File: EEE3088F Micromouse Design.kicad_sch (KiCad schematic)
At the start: 65 parts, among them J1 Conn_02x16_Odd_Even, J2 Conn_01x02, J3 TYPE-C-31-M-12, Q2 AO3400A, SW1 SW_SPDT, U1 INA219AxD, U11 DRV8833PW, U12 DRV8833PW, U13 AP22966DC8-7, U15 TP4056-42-ESOP8, U6 TPS5430DDA, U7 TPS61088RHLR, U9 CH224K

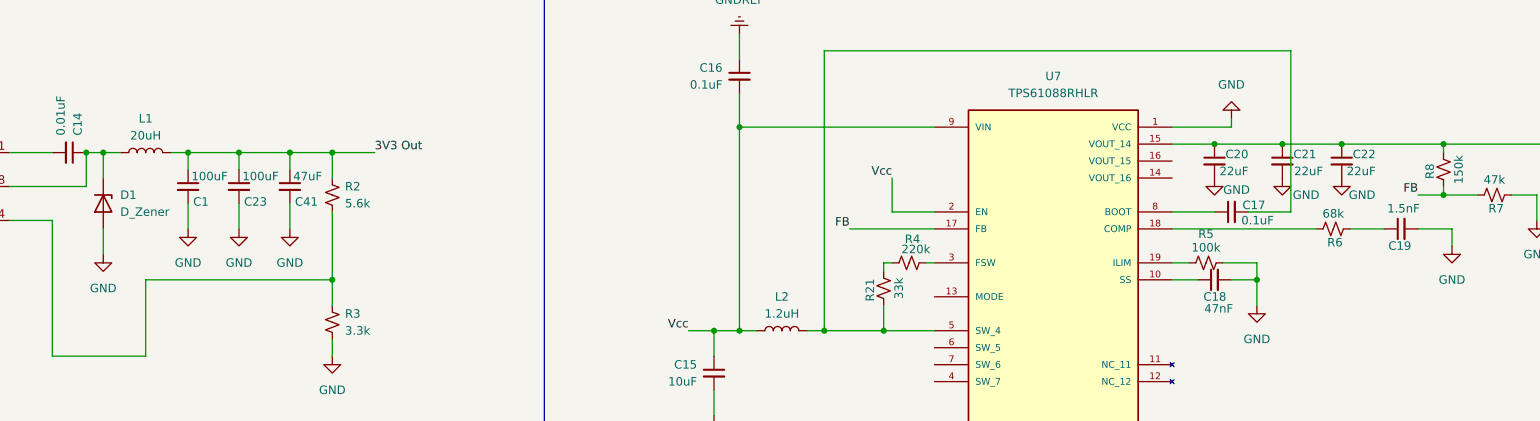
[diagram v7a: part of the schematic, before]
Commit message: Added footprints to 2 of 3 subcircuits
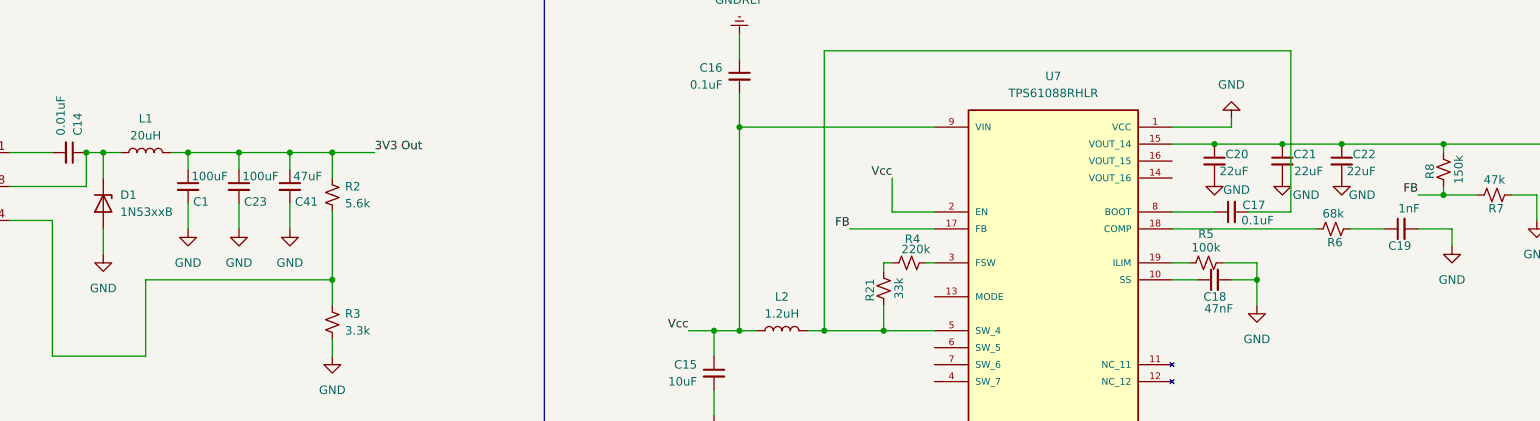
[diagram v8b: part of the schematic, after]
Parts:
- removed D1: D_Zener, symbol Device:D_Zener
- added D1: 1N53xxB, Inductor_1.2uH:L_custom_SMD, symbol Diode:1N53xxB
- C1, C23: footprint (none) -> Capacitor_SMD:C_1206_3216Metric_Pad1.33x1.80mm_HandSolder
- C14: footprint Capacitor_SMD:C_0402_1005Metric_Pad0.74x0.62mm_HandSolder -> Capacitor_SMD:C_0805_2012Metric_Pad1.18x1.45mm_HandSolder
- C15, C20: footprint Capacitor_SMD:C_0402_1005Metric_Pad0.74x0.62mm_HandSolder -> Capacitor_SMD:C_1206_3216Metric
- C18: footprint Capacitor_SMD:C_0402_1005Metric_Pad0.74x0.62mm_HandSolder -> Capacitor_SMD:C_0603_1608Metric_Pad1.08x0.95mm_HandSolder
- C19: value 1.5nF -> 1nF; footprint Capacitor_SMD:C_0402_1005Metric_Pad0.74x0.62mm_HandSolder -> Capacitor_SMD:C_0805_2012Metric_Pad1.18x1.45mm_HandSolder
- C21, C22: footprint Capacitor_SMD:C_0402_1005Metric_Pad0.74x0.62mm_HandSolder -> Capacitor_SMD:C_1206_3216Metric_Pad1.33x1.80mm_HandSolder
- C41: footprint (none) -> Capacitor_SMD:C_0805_2012Metric_Pad1.18x1.45mm_HandSolder
- L1: footprint (none) -> Inductor_THT:L_Axial_L11.0mm_D4.5mm_P5.08mm_Vertical_Fastron_MECC
- L2: footprint (none) -> Inductor_SMD:L_Changjiang_FXL0420
- R1: footprint Resistor_SMD:R_1206_3216Metric_Pad1.30x1.75mm_HandSolder -> Resistor_SMD:R_2512_6332Metric
- R16: footprint Resistor_SMD:R_1206_3216Metric_Pad1.30x1.75mm_HandSolder -> Resistor_SMD:R_2512_6332Metric_Pad1.40x3.35mm_HandSolder
- R2, R3, R4, R7, R8: footprint Resistor_SMD:R_1206_3216Metric_Pad1.30x1.75mm_HandSolder -> Resistor_SMD:R_0805_2012Metric_Pad1.20x1.40mm_HandSolder
- R6: footprint Resistor_SMD:R_1206_3216Metric_Pad1.30x1.75mm_HandSolder -> Resistor_SMD:R_0805_2012Metric
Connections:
- net GND: now also D1.2 (A)
- net at C14.1, L1.1, U6.8 (PH): now also D1.1 (K)
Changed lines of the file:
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@@
 			)
 		)
-		(property "Footprint" ""
+		(property "Footprint" "Inductor_THT:L_Axial_L11.0mm_D4.5mm_P5.08mm_Vertical_Fastron_MECC"
 			(at 269.24 52.07 0)
 			(effects
@@
 			)
 		)
-		(property "Footprint" "Resistor_SMD:R_1206_3216Metric_Pad1.30x1.75mm_HandSolder"
+		(property "Footprint" "Resistor_SMD:R_0805_2012Metric_Pad1.20x1.40mm_HandSolder"
 			(at 383.54 68.58 0)
 			(effects
@@
 			)
 		)
-		(property "Footprint" "Capacitor_SMD:C_0402_1005Metric_Pad0.74x0.62mm_HandSolder"
+		(property "Footprint" "Capacitor_SMD:C_1206_3216Metric"
 			(at 429.26 53.34 0)
 			(effects
@@
 			)
 		)
-		(property "Footprint" "Capacitor_SMD:C_0402_1005Metric_Pad0.74x0.62mm_HandSolder"
+		(property "Footprint" "Capacitor_SMD:C_1206_3216Metric_Pad1.33x1.80mm_HandSolder"
 			(at 448.31 53.34 0)
 			(effects
@@
 			)
 		)
-		(property "Footprint" "Resistor_SMD:R_1206_3216Metric_Pad1.30x1.75mm_HandSolder"
+		(property "Footprint" "Resistor_SMD:R_0805_2012Metric_Pad1.20x1.40mm_HandSolder"
 			(at 471.17 58.42 0)
 			(effects
@@
 			)
 		)
-		(property "Footprint" "Resistor_SMD:R_1206_3216Metric_Pad1.30x1.75mm_HandSolder"
+		(property "Footprint" "Resistor_SMD:R_0805_2012Metric_Pad1.20x1.40mm_HandSolder"
 			(at 297.18 77.47 0)
 			(effects
@@
 			)
 		)
-		(property "Footprint" "Resistor_SMD:R_1206_3216Metric_Pad1.30x1.75mm_HandSolder"
+		(property "Footprint" "Resistor_SMD:R_0805_2012Metric_Pad1.20x1.40mm_HandSolder"
 			(at 463.55 54.61 0)
 			(effects
@@
 			)
 		)
-		(property "Footprint" "Capacitor_SMD:C_0402_1005Metric_Pad0.74x0.62mm_HandSolder"
+		(property "Footprint" "Capacitor_SMD:C_1206_3216Metric"
 			(at 354.33 85.09 0)
 			(effects
@@
 			)
 		)
-		(property "Footprint" ""
+		(property "Footprint" "Capacitor_SMD:C_1206_3216Metric_Pad1.33x1.80mm_HandSolder"
 			(at 275.59 57.15 0)
 			(effects
@@
 			)
 		)
-		(property "Footprint" "Capacitor_SMD:C_0402_1005Metric_Pad0.74x0.62mm_HandSolder"
+		(property "Footprint" "Capacitor_SMD:C_0603_1608Metric_Pad1.08x0.95mm_HandSolder"
 			(at 429.26 71.12 0)
 			(effects
@@
 			)
 		)
-		(property "Footprint" "Resistor_SMD:R_1206_3216Metric_Pad1.30x1.75mm_HandSolder"
+		(property "Footprint" "Resistor_SMD:R_0805_2012Metric_Pad1.20x1.40mm_HandSolder"
 			(at 297.18 58.42 0)
 			(effects
@@
 			)
 		)
-		(property "Footprint" "Resistor_SMD:R_1206_3216Metric_Pad1.30x1.75mm_HandSolder"
+		(property "Footprint" "Resistor_SMD:R_2512_6332Metric"
 			(at 130.81 62.23 0)
 			(effects
@@
 	)
 	(symbol
+		(lib_id "Diode:1N53xxB")
+		(at 262.89 59.69 270)
+		(unit 1)
+		(exclude_from_sim no)
+		(in_bom yes)
+		(on_board yes)
+		(dnp no)
+		(fields_autoplaced yes)
+		(property "Reference" "D1"
+			(at 265.43 58.4199 90)
+			(effects
+				(font
+					(size 1.27 1.27)
+				)
+				(justify left)
+			)
+		)
+		(property "Value" "1N53xxB"
+			(at 265.43 60.9599 90)
+			(effects
+				(font
+					(size 1.27 1.27)
+				)
+				(justify left)
+			)
+		)
+		(property "Footprint" "Inductor_1.2uH:L_custom_SMD"
+			(at 258.445 59.69 0)
+			(effects
+				(font
+					(size 1.27 1.27)
+				)
+				(hide yes)
+			)
+		)
+		(property "Datasheet" "https://diotec.com/tl_files/diotec/files/pdf/datasheets/1n5345b.pdf"
+			(at 262.89 59.69 0)
+			(effects
+				(font
+					(size 1.27 1.27)
+				)
+				(hide yes)
+			)
+		)
+		(property "Description" "5000mW Zener Diode, DO-201"
+			(at 262.89 59.69 0)
+			(effects
+				(font
+					(size 1.27 1.27)
+				)
+				(hide yes)
+			)
+		)
+		(pin "1"
+		)
+		(pin "2"
+		)
+		(instances
+			(project ""
+				(path "/9da86a77-c081-4eef-8f80-aa4f3cdcfcf8"
+					(reference "D1")
+					(unit 1)
+				)
+			)
+		)
+	)
+	(symbol
 		(lib_id "Device:C_Small")
 		(at 439.42 53.34 0)
@@
 			)
 		)
-		(property "Footprint" "Capacitor_SMD:C_0402_1005Metric_Pad0.74x0.62mm_HandSolder"
+		(property "Footprint" "Capacitor_SMD:C_1206_3216Metric_Pad1.33x1.80mm_HandSolder"
 			(at 439.42 53.34 0)
 			(effects
@@
 			)
 		)
-		(property "Footprint" ""
+		(property "Footprint" "Capacitor_SMD:C_1206_3216Metric_Pad1.33x1.80mm_HandSolder"
 			(at 283.21 57.15 0)
 			(effects
@@
 	)
 	(symbol
-		(lib_id "Device:D_Zener")
-		(at 262.89 59.69 270)
-		(unit 1)
-		(exclude_from_sim no)
-		(in_bom yes)
-		(on_board yes)
-		(dnp no)
-		(fields_autoplaced yes)
-		(property "Reference" "D1"
-			(at 265.43 58.4199 90)
-			(effects
-				(font
-					(size 1.27 1.27)
-				)
-				(justify left)
-			)
-		)
-		(property "Value" "D_Zener"
-			(at 265.43 60.9599 90)
-			(effects
-				(font
-					(size 1.27 1.27)
-				)
-				(justify left)
-			)
-		)
-		(property "Footprint" ""
-			(at 262.89 59.69 0)
-			(effects
-				(font
-					(size 1.27 1.27)
-				)
-				(hide yes)
-			)
-		)
-		(property "Datasheet" "~"
-			(at 262.89 59.69 0)
-			(effects
-				(font
-					(size 1.27 1.27)
-				)
-				(hide yes)
-			)
-		)
-		(property "Description" "Zener diode"
-			(at 262.89 59.69 0)
-			(effects
-				(font
-					(size 1.27 1.27)
-				)
-				(hide yes)
-			)
-		)
-		(pin "2"
-		)
-		(pin "1"
-		)
-		(instances
-			(project ""
-				(path "/9da86a77-c081-4eef-8f80-aa4f3cdcfcf8"
-					(reference "D1")
-					(unit 1)
-				)
-			)
-		)
-	)
-	(symbol
 		(lib_name "GND_12")
 		(lib_id "power:GND")
@@
 			)
 		)
-		(property "Footprint" ""
+		(property "Footprint" "Capacitor_SMD:C_0805_2012Metric_Pad1.18x1.45mm_HandSolder"
 			(at 290.83 57.15 0)
 			(effects
@@
 			)
 		)
-		(property "Footprint" "Resistor_SMD:R_1206_3216Metric_Pad1.30x1.75mm_HandSolder"
+		(property "Footprint" "Resistor_SMD:R_0805_2012Metric"
 			(at 447.04 63.5 0)
 			(effects
@@
 			)
 		)
-		(property "Footprint" "Resistor_SMD:R_1206_3216Metric_Pad1.30x1.75mm_HandSolder"
+		(property "Footprint" "Resistor_SMD:R_2512_6332Metric_Pad1.40x3.35mm_HandSolder"
 			(at 552.45 90.17 0)
 			(effects
@@
 			)
 		)
-		(property "Value" "1.5nF"
+		(property "Value" "1nF"
 			(at 459.994 60.452 90)
 			(effects
@@
 			)
 		)
-		(property "Footprint" "Capacitor_SMD:C_0402_1005Metric_Pad0.74x0.62mm_HandSolder"
+		(property "Footprint" "Capacitor_SMD:C_0805_2012Metric_Pad1.18x1.45mm_HandSolder"
 			(at 457.2 63.5 0)
 			(effects
@@
 			)
 		)
-		(property "Footprint" ""
+		(property "Footprint" "Inductor_SMD:L_Changjiang_FXL0420"
 			(at 364.49 78.74 0)
 			(effects
@@
 			)
 		)
-		(property "Datasheet" "~"
+		(property "Datasheet" "https://jlcpcb.com/api/file/downloadByFileSystemAccessId/8588909906216816640"
 			(at 364.49 78.74 0)
 			(effects
@@
 			)
 		)
-		(property "Footprint" "Capacitor_SMD:C_0402_1005Metric_Pad0.74x0.62mm_HandSolder"
+		(property "Footprint" "Capacitor_SMD:C_0805_2012Metric_Pad1.18x1.45mm_HandSolder"
 			(at 257.81 52.07 0)
 			(effects
